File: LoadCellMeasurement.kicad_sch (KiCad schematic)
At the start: 2 parts, among them J18 4-Pin Load Cell, J19 5-Pin Load Cell

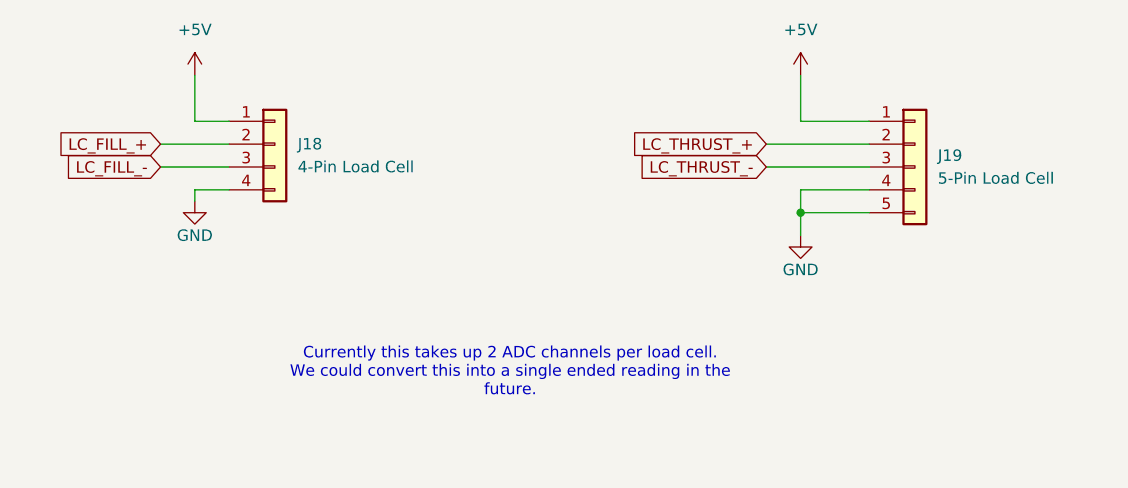
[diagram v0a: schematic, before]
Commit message: revamped schematic to be more readable
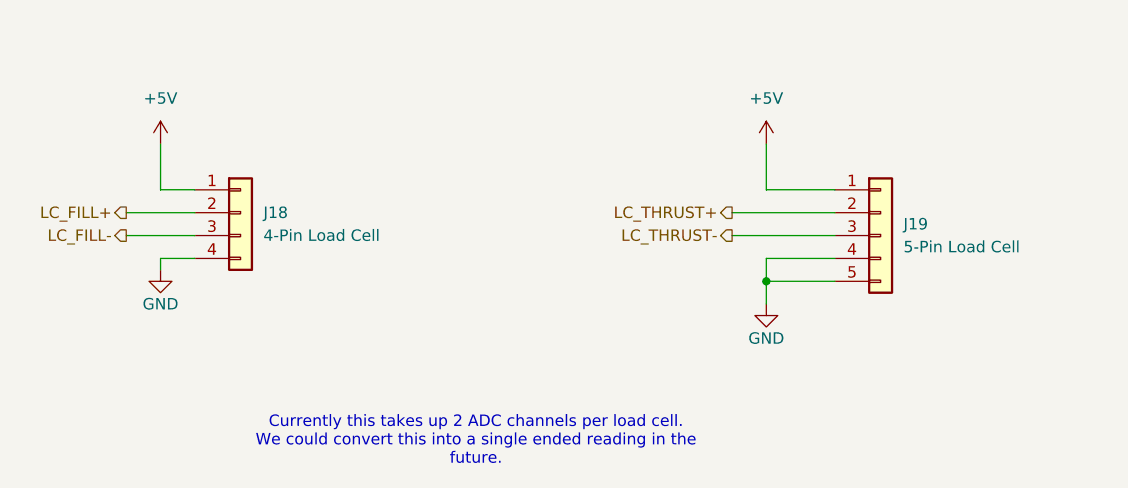
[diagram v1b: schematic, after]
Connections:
- net LC_FILL_+ renamed LC_FILL+
- net LC_FILL_- renamed LC_FILL-
- net LC_THRUST_+ renamed LC_THRUST+
- net LC_THRUST_- renamed LC_THRUST-
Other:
- moved on the sheet: J18, J19

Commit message: add 2 stage lockout to ignitor, add ignitor resistance reading with adc current source
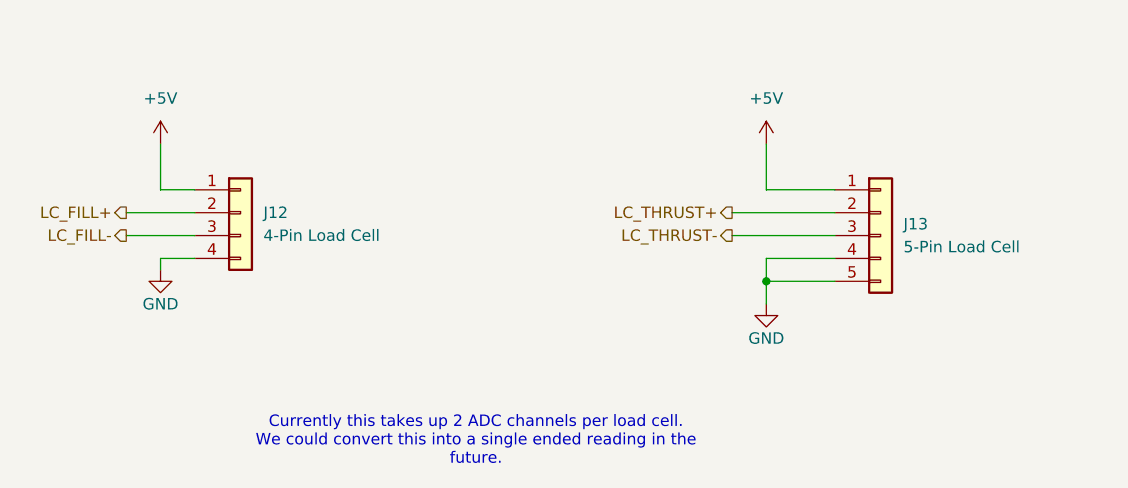
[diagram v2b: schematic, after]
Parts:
- renumbered J18 to J12, J19 to J13
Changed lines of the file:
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@@
 		(dnp no)
 		(fields_autoplaced yes)
-		(property "Reference" "J18"
+		(property "Reference" "J12"
 			(at 110.49 92.7099 0)
 			(effects
@@
 			(project ""
 				(path "/226c5870-4123-4efa-a2b3-b42d02f59bb7/5c3abfb7-eebf-4fa0-8883-27f893278ab8"
-					(reference "J18")
+					(reference "J12")
 					(unit 1)
 				)
@@
 		(on_board yes)
 		(dnp no)
-		(property "Reference" "#PWR0112"
+		(property "Reference" "#PWR0158"
 			(at 99.06 105.41 0)
 			(effects
@@
 			(project "nexus"
 				(path "/226c5870-4123-4efa-a2b3-b42d02f59bb7/5c3abfb7-eebf-4fa0-8883-27f893278ab8"
-					(reference "#PWR0112")
+					(reference "#PWR0158")
 					(unit 1)
 				)
@@
 		(dnp no)
 		(fields_autoplaced yes)
-		(property "Reference" "#PWR0111"
+		(property "Reference" "#PWR0157"
 			(at 99.06 88.9 0)
 			(effects
@@
 			(project ""
 				(path "/226c5870-4123-4efa-a2b3-b42d02f59bb7/5c3abfb7-eebf-4fa0-8883-27f893278ab8"
-					(reference "#PWR0111")
+					(reference "#PWR0157")
 					(unit 1)
 				)
@@
 		(on_board yes)
 		(dnp no)
-		(property "Reference" "#PWR0114"
+		(property "Reference" "#PWR0160"
 			(at 166.37 109.22 0)
 			(effects
@@
 			(project "nexus"
 				(path "/226c5870-4123-4efa-a2b3-b42d02f59bb7/5c3abfb7-eebf-4fa0-8883-27f893278ab8"
-					(reference "#PWR0114")
+					(reference "#PWR0160")
 					(unit 1)
 				)
@@
 		(dnp no)
 		(fields_autoplaced yes)
-		(property "Reference" "J19"
+		(property "Reference" "J13"
 			(at 181.61 93.9799 0)
 			(effects
@@
 			(project ""
 				(path "/226c5870-4123-4efa-a2b3-b42d02f59bb7/5c3abfb7-eebf-4fa0-8883-27f893278ab8"
-					(reference "J19")
+					(reference "J13")
 					(unit 1)
 				)
@@
 		(dnp no)
 		(fields_autoplaced yes)
-		(property "Reference" "#PWR0113"
+		(property "Reference" "#PWR0159"
 			(at 166.37 88.9 0)
 			(effects
@@
 			(project "panda"
 				(path "/226c5870-4123-4efa-a2b3-b42d02f59bb7/5c3abfb7-eebf-4fa0-8883-27f893278ab8"
-					(reference "#PWR0113")
-					(unit 1)
-				)
+					(reference "#PWR0159")
+					(unit 1)
+				)

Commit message: add capacitor and resistor footprints
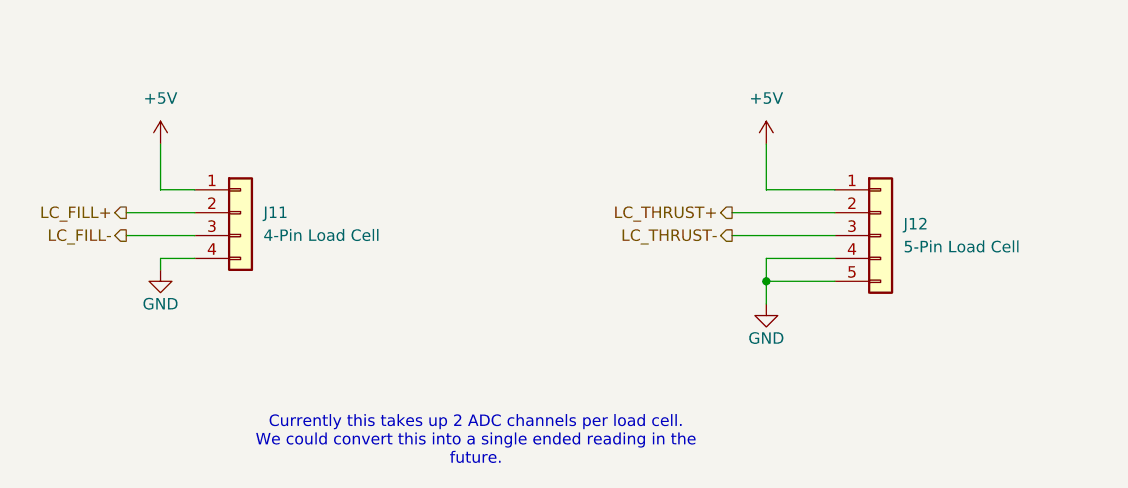
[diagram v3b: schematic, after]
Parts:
- renumbered J12 to J11, J13 to J12
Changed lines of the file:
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@@
 		(dnp no)
 		(fields_autoplaced yes)
-		(property "Reference" "J12"
+		(property "Reference" "J11"
 			(at 110.49 92.7099 0)
 			(effects
@@
 		)
 		(property "Description" "Generic connector, single row, 01x04, script generated (kicad-library-utils/schlib/autogen/connector/)"
+			(at 107.95 92.71 0)
+			(effects
+				(font
+					(size 1.27 1.27)
+				)
+				(hide yes)
+			)
+		)
+		(property "ADC Number" ""
+			(at 107.95 92.71 0)
+			(effects
+				(font
+					(size 1.27 1.27)
+				)
+				(hide yes)
+			)
+		)
+		(property "DCR" ""
+			(at 107.95 92.71 0)
+			(effects
+				(font
+					(size 1.27 1.27)
+				)
+				(hide yes)
+			)
+		)
+		(property "I2C Address" ""
+			(at 107.95 92.71 0)
+			(effects
+				(font
+					(size 1.27 1.27)
+				)
+				(hide yes)
+			)
+		)
+		(property "Irated" ""
+			(at 107.95 92.71 0)
+			(effects
+				(font
+					(size 1.27 1.27)
+				)
+				(hide yes)
+			)
+		)
+		(property "Isat" ""
+			(at 107.95 92.71 0)
+			(effects
+				(font
+					(size 1.27 1.27)
+				)
+				(hide yes)
+			)
+		)
+		(property "MFG" ""
+			(at 107.95 92.71 0)
+			(effects
+				(font
+					(size 1.27 1.27)
+				)
+				(hide yes)
+			)
+		)
+		(property "MFR" ""
 			(at 107.95 92.71 0)
 			(effects
@@
 			(project ""
 				(path "/226c5870-4123-4efa-a2b3-b42d02f59bb7/5c3abfb7-eebf-4fa0-8883-27f893278ab8"
-					(reference "J12")
+					(reference "J11")
 					(unit 1)
 				)
@@
 		(on_board yes)
 		(dnp no)
-		(property "Reference" "#PWR0158"
+		(property "Reference" "#PWR0156"
 			(at 99.06 105.41 0)
 			(effects
@@
 			(project "nexus"
 				(path "/226c5870-4123-4efa-a2b3-b42d02f59bb7/5c3abfb7-eebf-4fa0-8883-27f893278ab8"
-					(reference "#PWR0158")
+					(reference "#PWR0156")
 					(unit 1)
 				)
@@
 		(dnp no)
 		(fields_autoplaced yes)
-		(property "Reference" "#PWR0157"
+		(property "Reference" "#PWR0155"
 			(at 99.06 88.9 0)
 			(effects
@@
 			(project ""
 				(path "/226c5870-4123-4efa-a2b3-b42d02f59bb7/5c3abfb7-eebf-4fa0-8883-27f893278ab8"
-					(reference "#PWR0157")
+					(reference "#PWR0155")
 					(unit 1)
 				)
@@
 		(on_board yes)
 		(dnp no)
-		(property "Reference" "#PWR0160"
+		(property "Reference" "#PWR0158"
 			(at 166.37 109.22 0)
 			(effects
@@
 			(project "nexus"
 				(path "/226c5870-4123-4efa-a2b3-b42d02f59bb7/5c3abfb7-eebf-4fa0-8883-27f893278ab8"
-					(reference "#PWR0160")
+					(reference "#PWR0158")
 					(unit 1)
 				)
@@
 		(dnp no)
 		(fields_autoplaced yes)
-		(property "Reference" "J13"
+		(property "Reference" "J12"
 			(at 181.61 93.9799 0)
 			(effects
@@
 		)
 		(property "Description" "Generic connector, single row, 01x05, script generated (kicad-library-utils/schlib/autogen/connector/)"
+			(at 179.07 95.25 0)
+			(effects
+				(font
+					(size 1.27 1.27)
+				)
+				(hide yes)
+			)
+		)
+		(property "ADC Number" ""
+			(at 179.07 95.25 0)
+			(effects
+				(font
+					(size 1.27 1.27)
+				)
+				(hide yes)
+			)
+		)
+		(property "DCR" ""
+			(at 179.07 95.25 0)
+			(effects
+				(font
+					(size 1.27 1.27)
+				)
+				(hide yes)
+			)
+		)
+		(property "I2C Address" ""
+			(at 179.07 95.25 0)
+			(effects
+				(font
+					(size 1.27 1.27)
+				)
+				(hide yes)
+			)
+		)
+		(property "Irated" ""
+			(at 179.07 95.25 0)
+			(effects
+				(font
+					(size 1.27 1.27)
+				)
+				(hide yes)
+			)
+		)
+		(property "Isat" ""
+			(at 179.07 95.25 0)
+			(effects
+				(font
+					(size 1.27 1.27)
+				)
+				(hide yes)
+			)
+		)
+		(property "MFG" ""
+			(at 179.07 95.25 0)
+			(effects
+				(font
+					(size 1.27 1.27)
+				)
+				(hide yes)
+			)
+		)
+		(property "MFR" ""
 			(at 179.07 95.25 0)
 			(effects
@@
 			(project ""
 				(path "/226c5870-4123-4efa-a2b3-b42d02f59bb7/5c3abfb7-eebf-4fa0-8883-27f893278ab8"
-					(reference "J13")
+					(reference "J12")
 					(unit 1)
 				)
@@
 		(dnp no)
 		(fields_autoplaced yes)
-		(property "Reference" "#PWR0159"
+		(property "Reference" "#PWR0157"
 			(at 166.37 88.9 0)
 			(effects
@@
 			(project "panda"
 				(path "/226c5870-4123-4efa-a2b3-b42d02f59bb7/5c3abfb7-eebf-4fa0-8883-27f893278ab8"
-					(reference "#PWR0159")
+					(reference "#PWR0157")
 					(unit 1)
 				)

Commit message: change clamping resistors on tc adcs for lower leakage current
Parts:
- J11: footprint Connector_JST:JST_XH_B4B-XH-A_1x04_P2.50mm_Vertical -> Connector_Molex:Molex_Micro-Fit_3.0_43650-0415_1x04_P3.00mm_Vertical
- J12: footprint Connector_JST:JST_XH_B5B-XH-A_1x05_P2.50mm_Vertical -> Connector_Molex:Molex_Micro-Fit_3.0_43650-0515_1x05_P3.00mm_Vertical
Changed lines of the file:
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@@
 			)
 		)
-		(property "Footprint" "Connector_JST:JST_XH_B4B-XH-A_1x04_P2.50mm_Vertical"
+		(property "Footprint" "Connector_Molex:Molex_Micro-Fit_3.0_43650-0415_1x04_P3.00mm_Vertical"
 			(at 107.95 92.71 0)
 			(effects
@@
 		(on_board yes)
 		(dnp no)
-		(property "Reference" "#PWR0156"
+		(property "Reference" "#PWR0157"
 			(at 99.06 105.41 0)
 			(effects
@@
 			(project "nexus"
 				(path "/226c5870-4123-4efa-a2b3-b42d02f59bb7/5c3abfb7-eebf-4fa0-8883-27f893278ab8"
-					(reference "#PWR0156")
+					(reference "#PWR0157")
 					(unit 1)
 				)
@@
 		(dnp no)
 		(fields_autoplaced yes)
-		(property "Reference" "#PWR0155"
+		(property "Reference" "#PWR0156"
 			(at 99.06 88.9 0)
 			(effects
@@
 			(project ""
 				(path "/226c5870-4123-4efa-a2b3-b42d02f59bb7/5c3abfb7-eebf-4fa0-8883-27f893278ab8"
-					(reference "#PWR0155")
+					(reference "#PWR0156")
 					(unit 1)
 				)
@@
 		(on_board yes)
 		(dnp no)
-		(property "Reference" "#PWR0158"
+		(property "Reference" "#PWR0159"
 			(at 166.37 109.22 0)
 			(effects
@@
 			(project "nexus"
 				(path "/226c5870-4123-4efa-a2b3-b42d02f59bb7/5c3abfb7-eebf-4fa0-8883-27f893278ab8"
-					(reference "#PWR0158")
+					(reference "#PWR0159")
 					(unit 1)
 				)
@@
 			)
 		)
-		(property "Footprint" "Connector_JST:JST_XH_B5B-XH-A_1x05_P2.50mm_Vertical"
+		(property "Footprint" "Connector_Molex:Molex_Micro-Fit_3.0_43650-0515_1x05_P3.00mm_Vertical"
 			(at 179.07 95.25 0)
 			(effects
@@
 		(dnp no)
 		(fields_autoplaced yes)
-		(property "Reference" "#PWR0157"
+		(property "Reference" "#PWR0158"
 			(at 166.37 88.9 0)
 			(effects
@@
 			(project "panda"
 				(path "/226c5870-4123-4efa-a2b3-b42d02f59bb7/5c3abfb7-eebf-4fa0-8883-27f893278ab8"
-					(reference "#PWR0157")
-					(unit 1)
-				)
+					(reference "#PWR0158")
+					(unit 1)
+				)

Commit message: Update version number in KiCad files
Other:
- title: Load Cell Measurement -> PANDA
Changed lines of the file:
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@@
 	(paper "A4")
 	(title_block
-		(title "Load Cell Measurement")
-		(rev "1.0.0")
+		(title "PANDA")
+		(date "2025-12-21")
+		(rev "3.0.0")
 		(company "Queen's Rocket Engineering Team")
 	)
